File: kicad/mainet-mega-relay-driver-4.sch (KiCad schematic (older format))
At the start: 8 parts, among them J33 Screw_Terminal_01x03, K4 SANYOU_SRD_Form_C, Q4 2N3904, U5 4N37

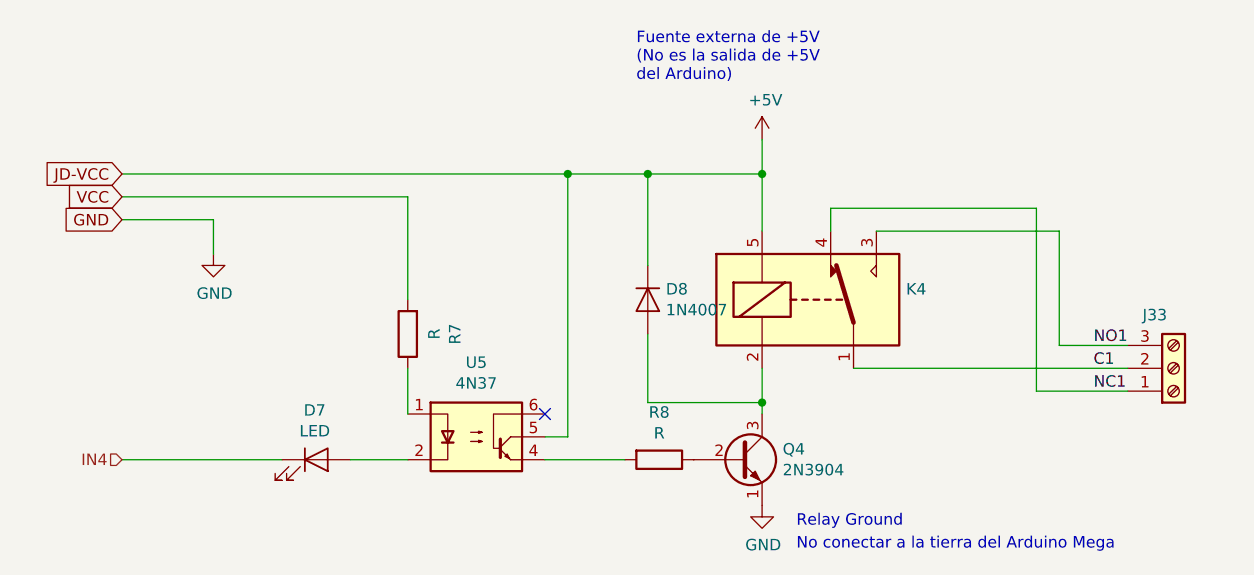
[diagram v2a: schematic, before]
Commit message: KICAD: Actualización de esquematicos del módulo de 8 relés de control
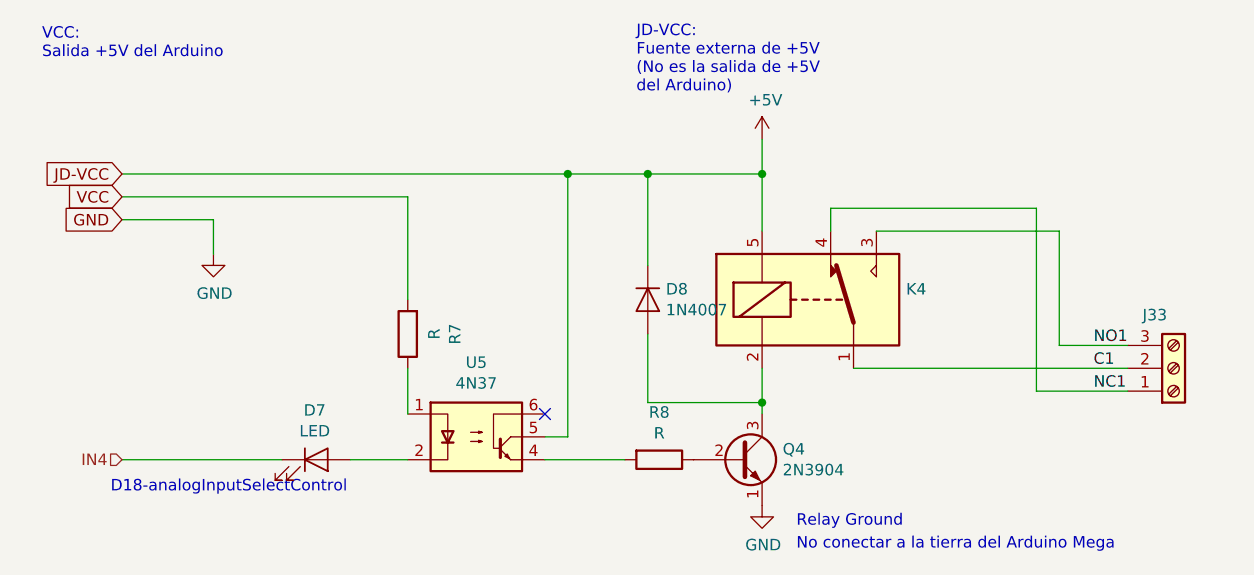
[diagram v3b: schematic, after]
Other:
- note added: "D18-analogInputSelectControl"
- note added: "JD-VCC:\nFuente externa de +5V\n(No es la salida de +5V \ndel Arduino)"
- note added: "VCC:\nSalida +5V del Arduino"
- note removed: "Fuente externa de +5V\n(No es la salida de +5V \ndel Arduino)"
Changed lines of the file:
@@
 EESchema Schematic File Version 4
 LIBS:mainet-mega-cache
-LIBS:mainet-mega-5V-to-mp-10v-cache
 EELAYER 30 0
 EELAYER END
@@
 encoding utf-8
 Sheet 10 21
-Title ""
-Date ""
+Title "Relay driver 4"
+Date "2021-02-02"
 Rev ""
 Comp ""
@@
 	1    0    0    -1
 $EndComp
-Text Notes 5850 2550 0    50   ~ 0
-Fuente externa de +5V\n(No es la salida de +5V \ndel Arduino)
 Text Notes 6550 4500 0    50   ~ 0
 Relay Ground\n
@@
 Text GLabel 3600 3150 0    50   Input ~ 0
 GND
+Text Notes 5850 2600 0    50   ~ 0
+JD-VCC:\nFuente externa de +5V\n(No es la salida de +5V \ndel Arduino)
+Text Notes 3250 2450 0    50   ~ 0
+VCC:\nSalida +5V del Arduino
+Text Notes 3550 4350 0    50   ~ 0
+D18-analogInputSelectControl
 $EndSCHEMATC
